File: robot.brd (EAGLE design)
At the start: 63.2 x 48.2 mm, 18 parts

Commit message: new added vias
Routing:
- net 0: track 20.7 -> 23.3 mm, vias 9 -> 11
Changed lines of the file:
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@@
 <via x="46.99" y="60.96" extent="1-16" drill="0.35"/>
 <wire x1="46.99" y1="62.55" x2="46.99" y2="60.96" width="0.254" layer="1"/>
-<wire x1="7.94" y1="30.48" x2="13.97" y2="30.25" width="0" layer="19" extent="1-1"/>
+<wire x1="14.92" y1="31.0032" x2="14.92" y2="32.192" width="0.1524" layer="1"/>
+<wire x1="14.92" y1="32.192" x2="14.986" y2="32.258" width="0.1524" layer="1"/>
+<wire x1="14.92" y1="31.0032" x2="14.92" y2="29.784" width="0.1524" layer="1"/>
+<wire x1="14.92" y1="29.784" x2="14.986" y2="29.718" width="0.1524" layer="1"/>
+<via x="14.986" y="32.258" extent="1-16" drill="0.2"/>
+<via x="14.986" y="29.718" extent="1-16" drill="0.2"/>
 </signal>
 <signal name="N$4">
@@
 <wire x1="45.4" y1="66.04" x2="46.99" y2="64.45" width="0.254" layer="1"/>
 </signal>
-<signal name="N$5">
-<via x="14.986" y="31.496" extent="1-16" drill="0.2"/>
-</signal>
-<signal name="N$6">
-<via x="14.986" y="30.48" extent="1-16" drill="0.2"/>
-</signal>
 </signals>

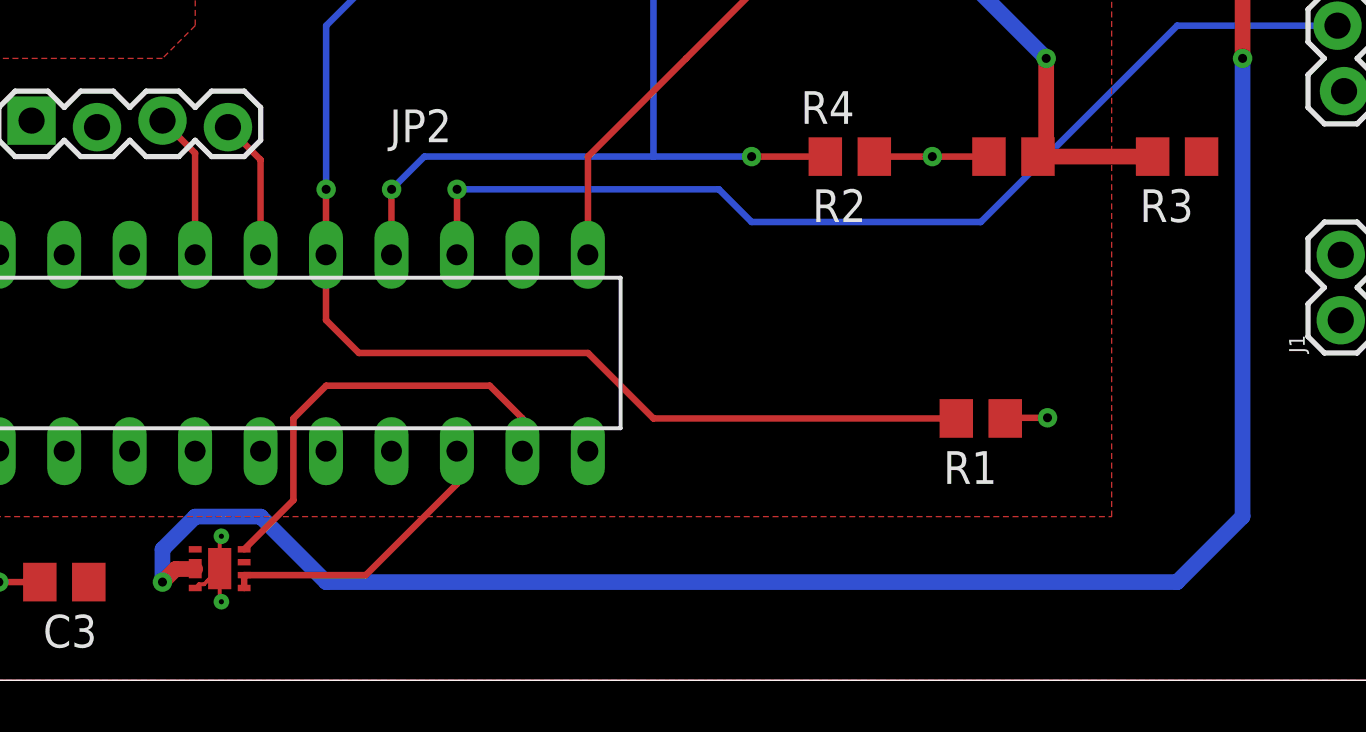
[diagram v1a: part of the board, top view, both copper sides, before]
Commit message: Adding the STL files for 3D printing the chassis.
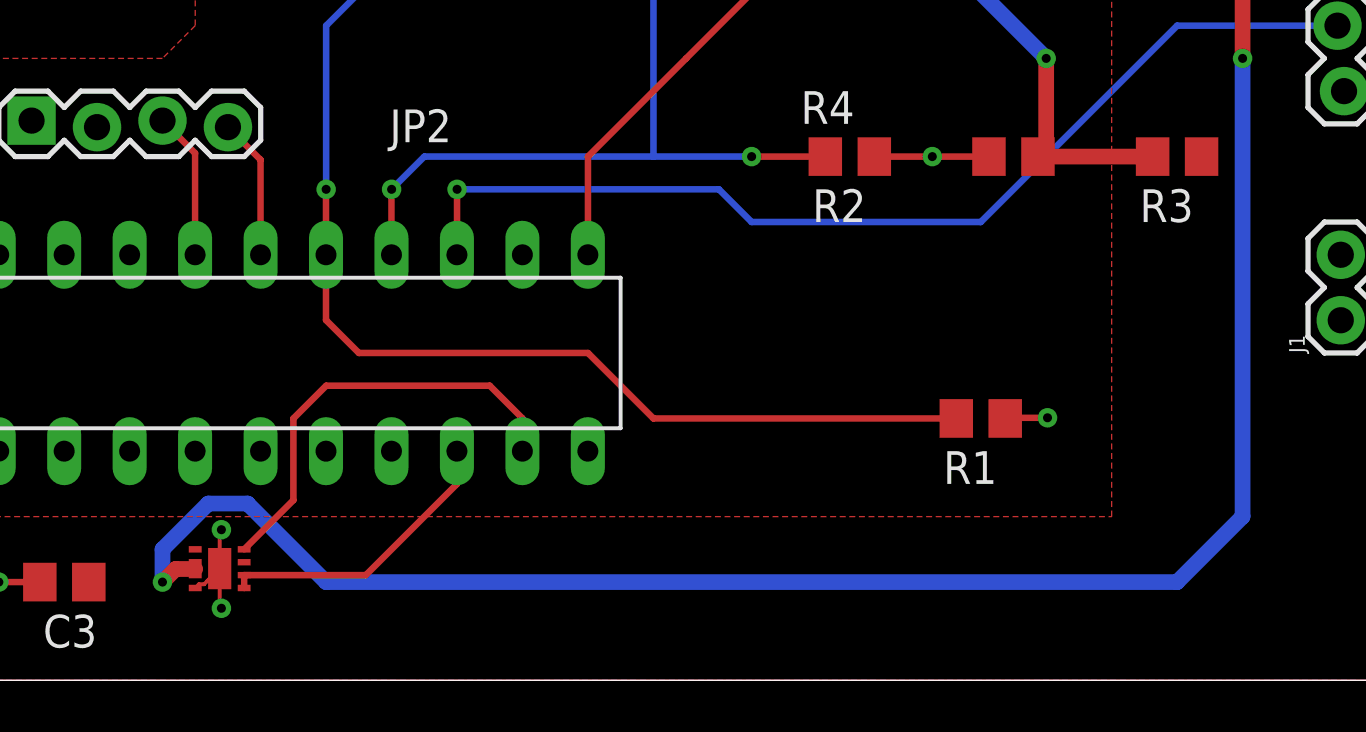
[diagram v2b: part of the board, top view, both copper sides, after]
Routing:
- net 4V5: track 0.68 -> 0.00 mm
- net 0: track 23.3 -> 23.9 mm
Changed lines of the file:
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@@
 <via x="46.99" y="60.96" extent="1-16" drill="0.35"/>
 <wire x1="46.99" y1="62.55" x2="46.99" y2="60.96" width="0.254" layer="1"/>
-<wire x1="14.92" y1="31.0032" x2="14.92" y2="32.192" width="0.1524" layer="1"/>
-<wire x1="14.92" y1="32.192" x2="14.986" y2="32.258" width="0.1524" layer="1"/>
-<wire x1="14.92" y1="31.0032" x2="14.92" y2="29.784" width="0.1524" layer="1"/>
-<wire x1="14.92" y1="29.784" x2="14.986" y2="29.718" width="0.1524" layer="1"/>
-<via x="14.986" y="32.258" extent="1-16" drill="0.2"/>
-<via x="14.986" y="29.718" extent="1-16" drill="0.2"/>
+<wire x1="14.92" y1="31.0032" x2="14.92" y2="32.512" width="0.1524" layer="1"/>
+<wire x1="14.92" y1="32.512" x2="14.986" y2="32.512" width="0.1524" layer="1"/>
+<wire x1="14.92" y1="31.0032" x2="14.92" y2="29.53" width="0.1524" layer="1"/>
+<wire x1="14.92" y1="29.53" x2="14.986" y2="29.464" width="0.1524" layer="1"/>
+<via x="14.986" y="32.512" extent="1-16" drill="0.35"/>
+<via x="14.986" y="29.464" extent="1-16" drill="0.35"/>
 </signal>
 <signal name="N$4">
@@
 <via x="12.7" y="30.48" extent="1-16" drill="0.35"/>
 <wire x1="12.7" y1="30.48" x2="12.7" y2="31.75" width="0.6096" layer="16"/>
-<wire x1="12.7" y1="31.75" x2="13.97" y2="33.02" width="0.6096" layer="16"/>
-<wire x1="13.97" y1="33.02" x2="16.51" y2="33.02" width="0.6096" layer="16"/>
-<wire x1="16.51" y1="33.02" x2="19.05" y2="30.48" width="0.6096" layer="16"/>
+<wire x1="12.7" y1="31.75" x2="14.478" y2="33.528" width="0.6096" layer="16"/>
+<wire x1="14.478" y1="33.528" x2="16.002" y2="33.528" width="0.6096" layer="16"/>
+<wire x1="16.002" y1="33.528" x2="19.05" y2="30.48" width="0.6096" layer="16"/>
 <wire x1="19.05" y1="30.48" x2="52.07" y2="30.48" width="0.6096" layer="16"/>
 <wire x1="58.293" y1="58.42" x2="58.293" y2="57.15" width="0.6096" layer="1"/>
@@
 <contactref element="C1" pad="1"/>
 <contactref element="R3" pad="1"/>
-<wire x1="53.18" y1="46.83" x2="53.02" y2="46.99" width="0.1524" layer="1"/>
-<wire x1="53.02" y1="46.99" x2="53.34" y2="46.67" width="0.1524" layer="1"/>
 <polygon width="0.1524" layer="1">
 <vertex x="0" y="64.77"/>

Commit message: Added two-pin header to board for interface with BeagleBone.
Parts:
- added J3: (no value), SparkFun-Connectors:1X02
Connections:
- new net IO_1: J3.2, U$1.2
- new net IO_2: J3.1, U$1.3
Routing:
- net IO_2: track 0.00 -> 10.8 mm
- net IO_1: track 0.00 -> 8.00 mm
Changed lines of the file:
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@@
 <attribute name="VALUE" x="49.53" y="62.865" size="1.27" layer="27" rot="R90"/>
+</element>
+<element name="J3" library="SparkFun-Connectors" library_urn="urn:adsk.eagle:library:513" package="1X02" package3d_urn="urn:adsk.eagle:package:38039/1" value="" x="3.556" y="29.464" smashed="yes" rot="R90">
+<attribute name="NAME" x="2.159" y="28.194" size="0.6096" layer="25" font="vector" ratio="20" rot="R90"/>
+<attribute name="VALUE" x="5.588" y="28.194" size="0.6096" layer="27" font="vector" ratio="20" rot="R90"/>
 </element>
 </elements>
@@
 <wire x1="45.4" y1="66.04" x2="46.99" y2="64.45" width="0.254" layer="1"/>
 </signal>
+<signal name="IO_1">
+<contactref element="U$1" pad="2"/>
+<contactref element="J3" pad="2"/>
+<wire x1="3.556" y1="32.004" x2="4.318" y2="32.766" width="0.254" layer="1"/>
+<wire x1="4.318" y1="32.766" x2="8.128" y2="32.766" width="0.254" layer="1"/>
+<wire x1="8.128" y1="32.766" x2="8.89" y2="33.528" width="0.254" layer="1"/>
+<wire x1="8.89" y1="35.555" x2="8.885" y2="35.56" width="0.1524" layer="1"/>
+<wire x1="8.89" y1="33.528" x2="8.89" y2="35.555" width="0.254" layer="1"/>
+</signal>
+<signal name="IO_2">
+<contactref element="U$1" pad="3"/>
+<contactref element="J3" pad="1"/>
+<wire x1="11.425" y1="35.56" x2="11.425" y2="34.793" width="0.254" layer="1"/>
+<wire x1="11.425" y1="34.793" x2="8.636" y2="32.004" width="0.254" layer="1"/>
+<wire x1="6.096" y1="32.004" x2="3.556" y2="29.464" width="0.254" layer="1"/>
+<wire x1="8.636" y1="32.004" x2="6.096" y2="32.004" width="0.254" layer="1"/>
+</signal>
 </signals>
